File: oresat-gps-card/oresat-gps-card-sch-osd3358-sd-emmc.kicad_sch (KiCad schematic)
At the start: 66 parts, among them J4 DM3BT-DSF-PEJS, U1 OSD3358-512M-BSM, U24 25AAXX, U8 TCAN330, U9 EMMC+RESET+5.1-COMPATIBLE-BA

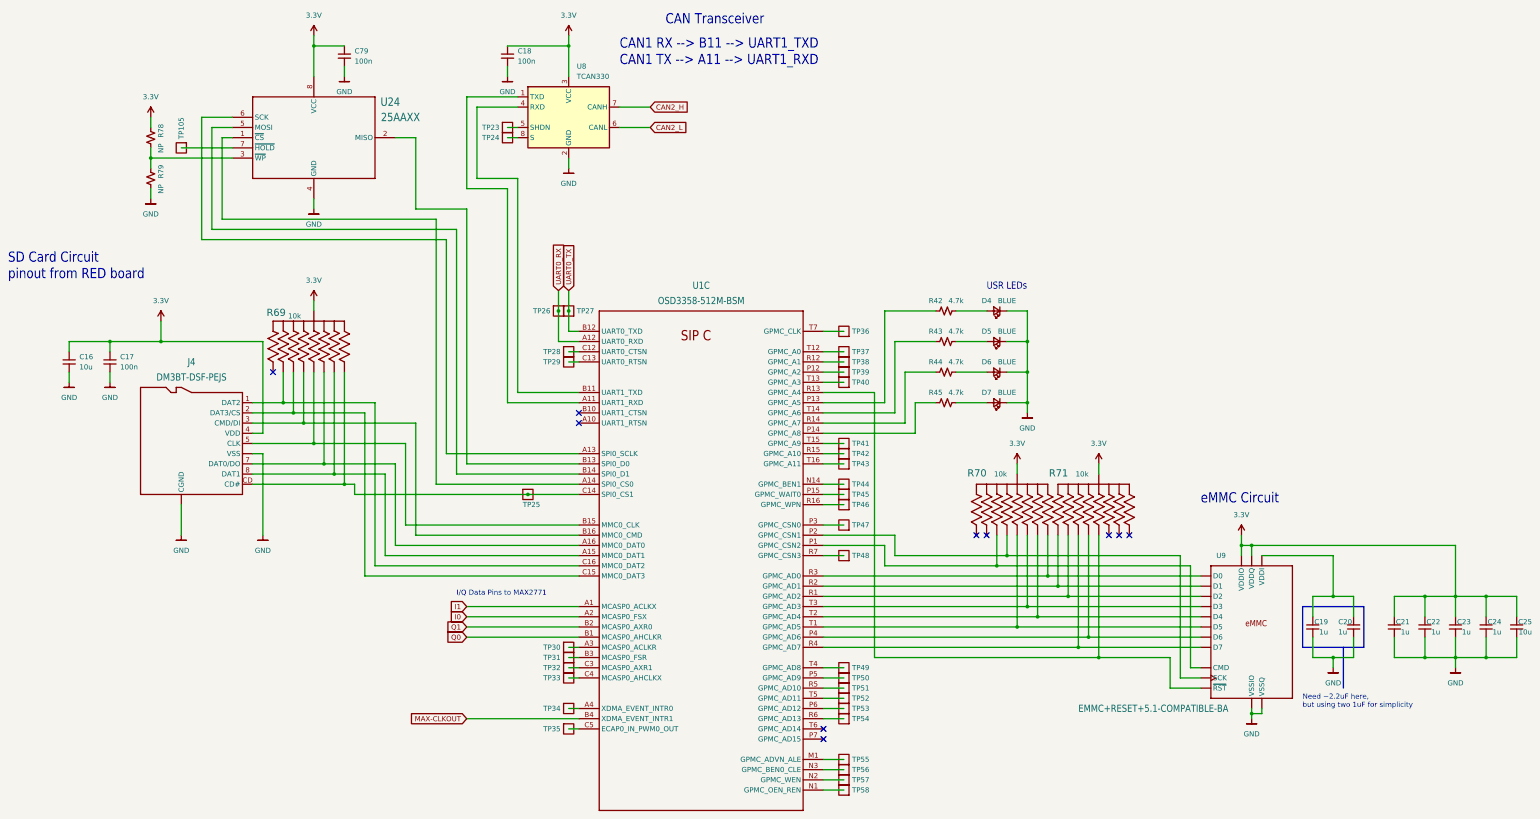
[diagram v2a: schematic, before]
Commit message: Updated GPS card with changes from C3 and notes. Fixed library issues
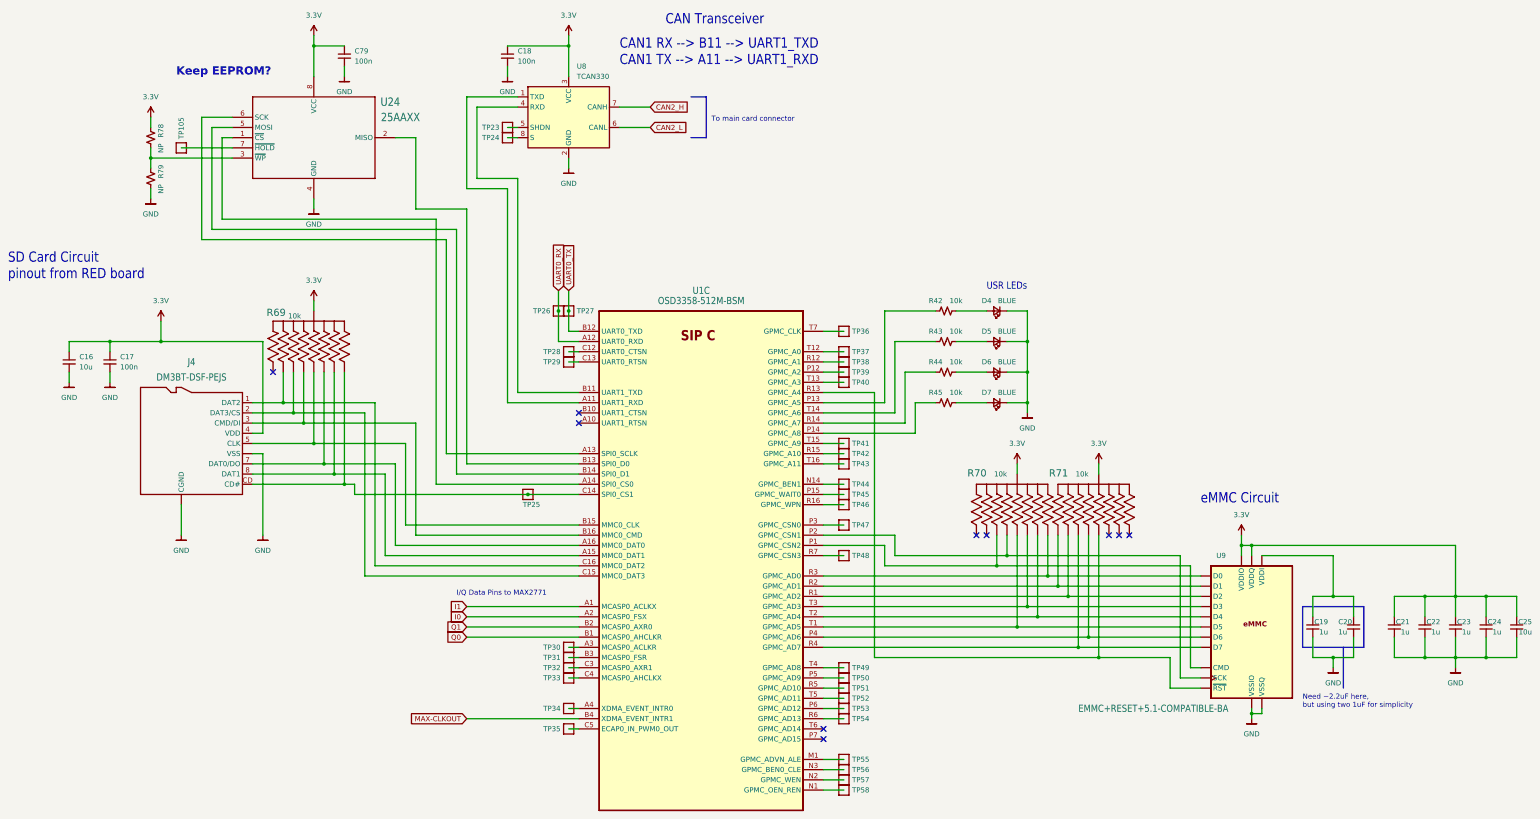
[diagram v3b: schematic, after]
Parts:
- J4: symbol J-Hirose-DM3BT-DSF-PEJS-sd-connector:DM3BT-DSF-PEJS -> oresat-connectors:DM3BT-DSF-PEJS
- R42, R43, R44, R45: value 4.7k -> 10k
- R69, R70, R71: footprint oresat-footprints:R-ARRAY_EXBA-M -> oresat-passives:Panasonic_Resistor_Array_EXBA10; symbol R-EXB-A10P391j:EXB-A10P391J -> oresat-passives:EXB-A10P391J
- TP105, TP23, TP24, TP25, TP26, TP27, TP28, TP29, TP30, TP31, TP32, TP33, TP34, TP35, TP36, TP37, TP38, TP39, TP40, TP41, TP42, TP43, TP44, TP45, TP46, TP47, TP48, TP49, TP50, TP51, TP52, TP53, TP54, TP55, TP56, TP57, TP58: value Test-Point -> 0.03x0.04; footprint OreSat-TestPoint:PAD.03X.04 -> oresat-misc:TestPoint_Pad_D1.0mm; symbol OreSat-TestPoint:Test-Point -> oresat-misc:Test-Point-1mm-round
- U1: footprint oresat-footprints:U-Octavo-OSD335X-BGA-256 -> oresat-ics:U-Octavo-OSD335X-BGA-256; symbol U-OSD3358-512M-BSM:OSD3358-512M-BSM -> oresat-ics:OSD3358-512M-BSM
- U24: symbol U-Microchip-25AAXXX-eeprom:25AAXX -> oresat-ics:25AAXX
- U9: footprint oresat-footprints:BGA-153(11.5X13)(EMMC-BA) -> oresat-ics:BGA-153(11.5X13)(EMMC-BA); symbol U-Generic-eMMC-153pin:EMMC+RESET+5.1-COMPATIBLE-BA -> oresat-ics:EMMC+RESET+5.1-COMPATIBLE-BA
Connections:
- net GND: now also U9.A12 (NC), U9.A13 (NC)
- net at C19.1, C20.1, U9.C2 (VDDI): now also U9.A2 (NC)
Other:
- note added: "Keep EEPROM?"
- note added: "To main card connector"

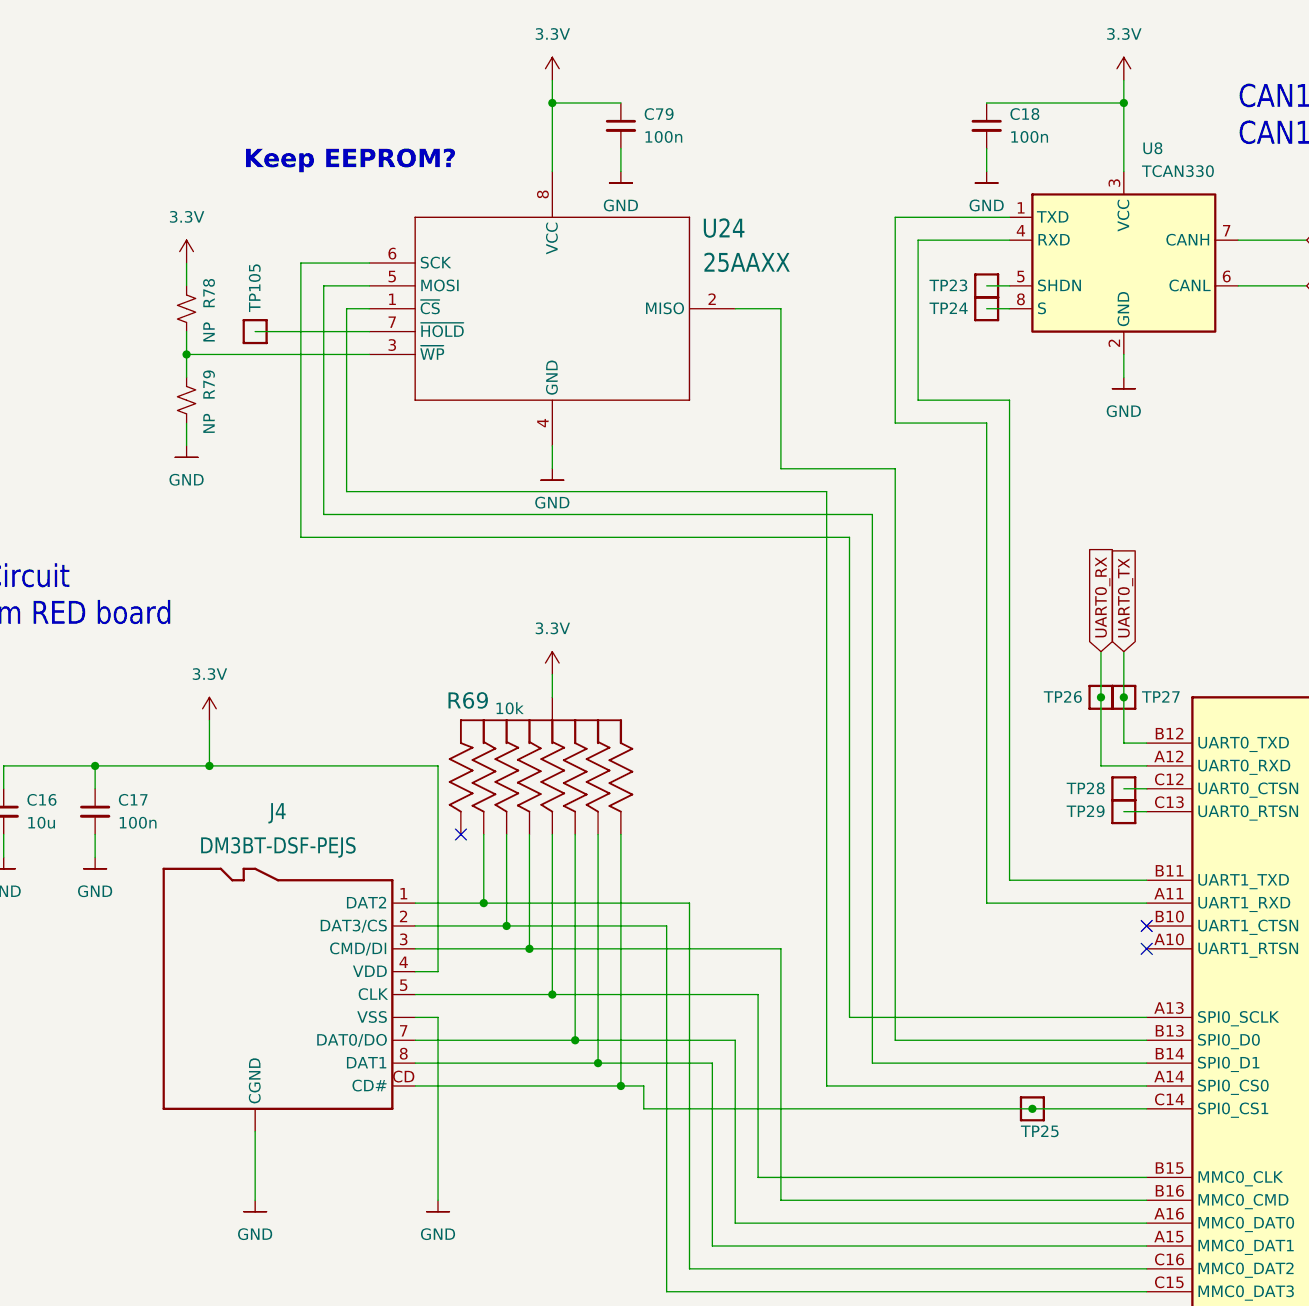
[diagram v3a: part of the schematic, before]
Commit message: Updated GPS card
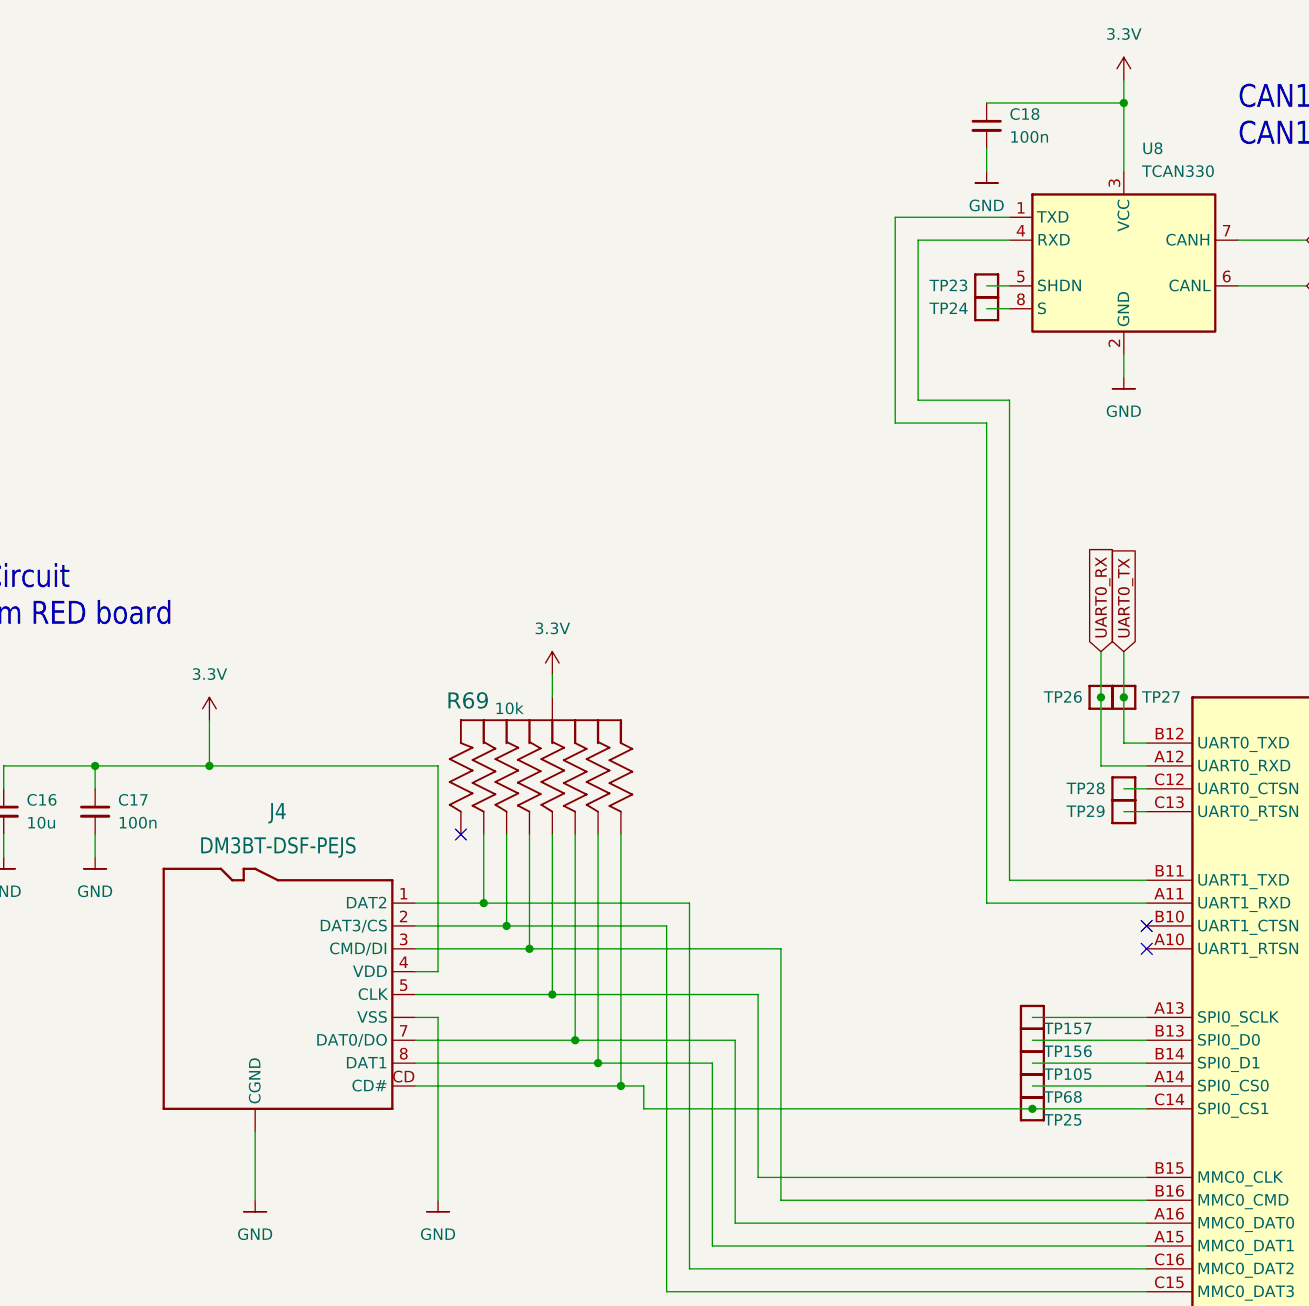
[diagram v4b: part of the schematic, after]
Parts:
- removed C79: 100n, Capacitor_SMD:C_0603_1608Metric, symbol Device:C_Small
- removed R78, R79: NP, Resistor_SMD:R_0603_1608Metric, symbol Device:R_Small_US
- removed U24: 25AAXX, Package_SO:SOIC-8_3.9x4.9mm_P1.27mm, symbol oresat-ics:25AAXX
- added TP156, TP157, TP68: 0.03x0.04, oresat-misc:TestPoint_Pad_D1.0mm, symbol oresat-misc:Test-Point-1mm-round
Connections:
- net at U1.A14 (SPI0_CS0): now also TP68.1
- net at U1.B13 (SPI0_D0): now also TP156.1
- net at U1.B14 (SPI0_D1): now also TP105.1
- net at U1.A13 (SPI0_SCLK): now also TP157.1
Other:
- note removed: "Keep EEPROM?"
